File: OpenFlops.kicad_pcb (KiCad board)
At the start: 2 copper layers, 111.6 x 59.4 mm, 87 parts, among them J99 OSHW_LOGO, P1 FLOPPY_CONN, P2 POWER_INPUT, P3 USB_A_FEMALE, P4 PROG_PORT, P5 JUMPER_JC, P6 ENCODER_PORT, P7 DISPLAY_PORT, P8 USB_HEADER, P9 EXTERNAL_SPEAKER, Q1 BSS138, Q2 BSS138, Q3 BSS138, Q4 BSS138, Q5 BSS138, Q6 BSS138, Q7 MMBT3904, U1 74HCT04, U3 STM32F105RBT6, U4 LM1117-3.3, Y1 8 MHz

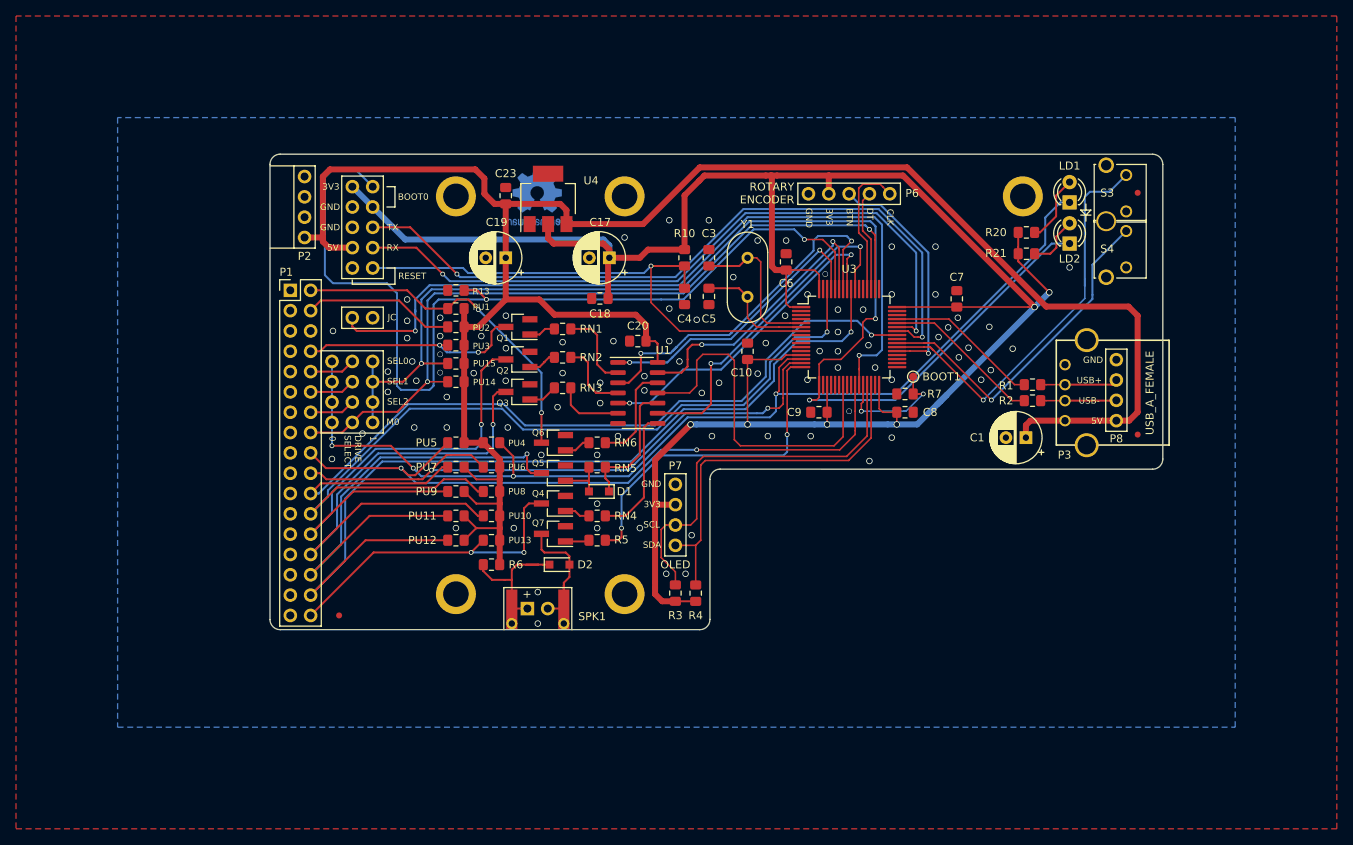
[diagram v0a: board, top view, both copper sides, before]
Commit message: Merge SD card changes from @COREi64; update to KiCad v8
This includes https://github.com/SukkoPera/OpenFlops/pull/18 from @COREi64 and updates the file formats to KiCad v8
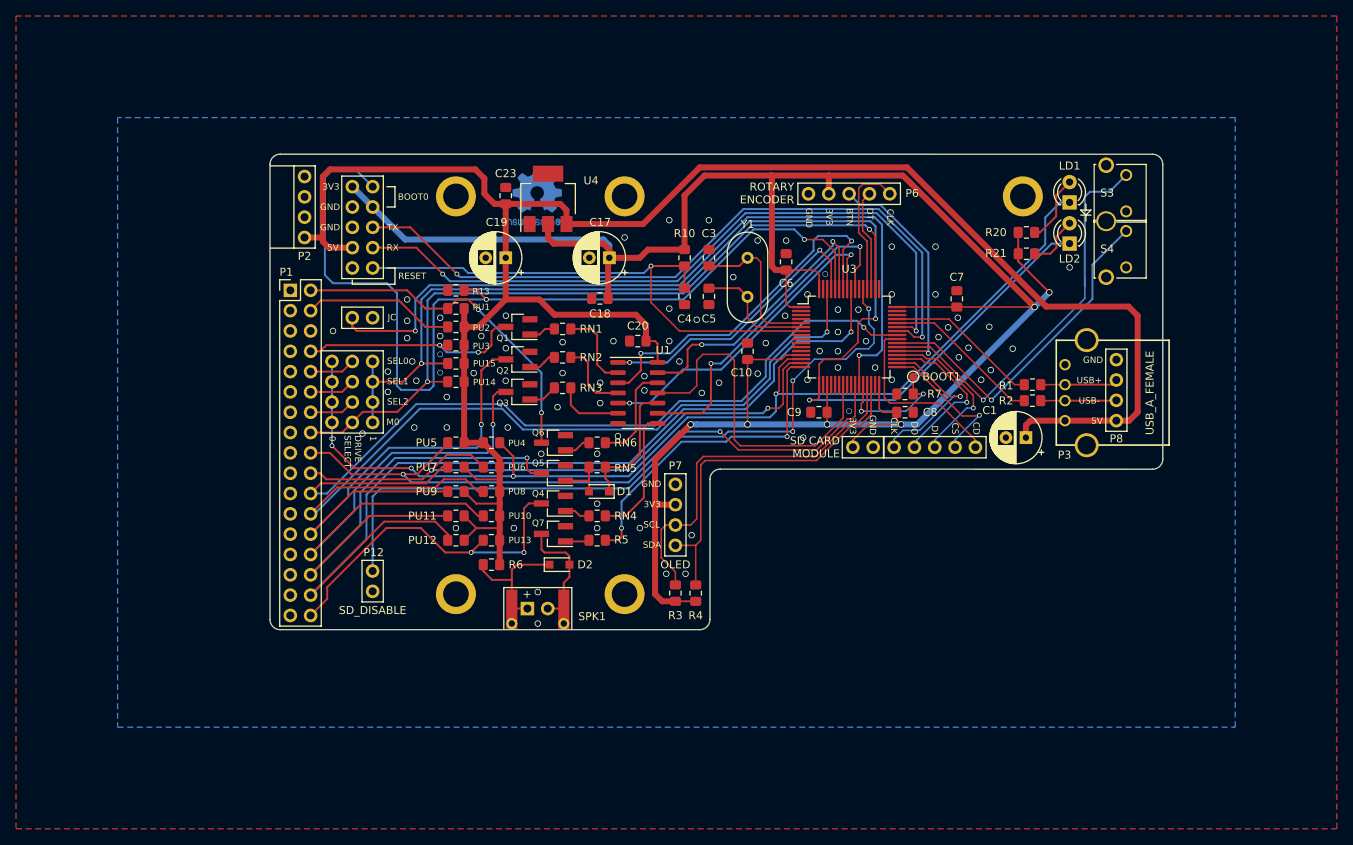
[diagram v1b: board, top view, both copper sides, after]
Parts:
- removed FID1, FID2, FID3: Fiducial, Fiducial:Fiducial_0.75mm_Mask1.5mm
- added P10: SD CARD, OpenFlops:PinHeader_1x05_P2.54mm_Vertical, F.Cu at (183.4, 92.0)
- added P11: SD PWR, OpenFlops:PinHeader_1x02_P2.54mm_Vertical, F.Cu at (170.7, 92.0)
- added P12: SD_DISABLE, OpenFlops:PinHeader_1x02_P2.54mm_Vertical, F.Cu at (108.1, 107.5)
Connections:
- net /~dskchg renamed /~{dskchg}
- net /~dskchg_3v3 renamed /~{dskchg_3v3}
- net /~index renamed /~{index}
- net /~index_3v3 renamed /~{index_3v3}
- net /~inuse renamed /~{inuse}
- net /~mtron renamed /~{mtron}
- net /~rdata renamed /~{rdata}
- net /~rdata_3v3 renamed /~{rdata_3v3}
- net /~rdy renamed /~{rdy}
- net /~rdy_3v3 renamed /~{rdy_3v3}
- net /~sel0 renamed /~{sel0}
- net /~sel1 renamed /~{sel1}
- net /~sel2 renamed /~{sel2}
- net /~selx renamed /~{selx}
- net /~sely renamed /~{sely}
- net /~side renamed /~{side}
- net /~step renamed /~{step}
- net /~trk0 renamed /~{trk0}
- net /~trk0_3v3 renamed /~{trk0_3v3}
- net /~wdata renamed /~{wdata}
- net /~wgate renamed /~{wgate}
- net /~wprot renamed /~{wprot}
- net /~wprot_3v3 renamed /~{wprot_3v3}
- P1 pad 6: (no net) -> /~{sel3}
- P2 pad 4: (no net) -> unconnected-(P2-Pad4)
- U3 pad 10: (no net) -> unconnected-(U3-Pad10)
- U3 pad 11: (no net) -> unconnected-(U3-Pad11)
- U3 pad 20: (no net) -> unconnected-(U3-Pad20)
- U3 pad 21: (no net) -> unconnected-(U3-Pad21)
- U3 pad 22: (no net) -> unconnected-(U3-Pad22)
- U3 pad 24: (no net) -> unconnected-(U3-Pad24)
- U3 pad 25: (no net) -> unconnected-(U3-Pad25)
- U3 pad 33: (no net) -> /spi_cs
- U3 pad 34: (no net) -> /spi_clk
- U3 pad 35: (no net) -> /spi_do
- U3 pad 36: (no net) -> /spi_di
- U3 pad 40: (no net) -> /spi_cd
- U3 pad 46: (no net) -> unconnected-(U3-Pad46)
- U3 pad 49: (no net) -> /swclk
- U3 pad 53: GND -> Net-(U3-Pad53)
- U3 pad 54: (no net) -> unconnected-(U3-Pad54)
- U3 pad 8: (no net) -> unconnected-(U3-Pad8)
- U3 pad 9: (no net) -> unconnected-(U3-Pad9)
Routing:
- net Net-(U3-Pad53): track 0.00 -> 91.0 mm, vias 0 -> 3
- net /spi_cd: track 0.00 -> 23.3 mm
- net /spi_clk: track 0.00 -> 21.1 mm, vias 0 -> 1
- net /spi_do: track 0.00 -> 20.8 mm, vias 0 -> 1
- net /spi_di: track 0.00 -> 20.6 mm, vias 0 -> 1
- net /spi_cs: track 0.00 -> 18.1 mm, vias 0 -> 1
- net +3V3: track 288.7 -> 296.7 mm
- net /~{rdy}: track 40.7 -> 43.4 mm
- net /~{rdata}: track 60.9 -> 59.1 mm
- net /spk+: track 18.6 -> 16.8 mm
- net /disp_dio: track 47.4 -> 45.7 mm
- net /disp_clk: track 49.0 -> 47.4 mm
- net /jb: track 42.4 -> 40.9 mm
- net /jc: track 99.9 -> 98.4 mm
- net /~{rdata_3v3}: track 44.8 -> 43.5 mm
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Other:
- net class Default removed
- net class Power removed
- net class uC removed
- board text added: "CD"
- board text added: "CS"
- board text added: "DI"
- board text added: "DO"
- board text added: "Licensed under CERN OHL v.1.3"
- board text added: "SD CARD MODULE"
- board text added: "V1.4"
- board text removed: "Licensed under CERN OHL v.1.2"
- board text removed: "V1"

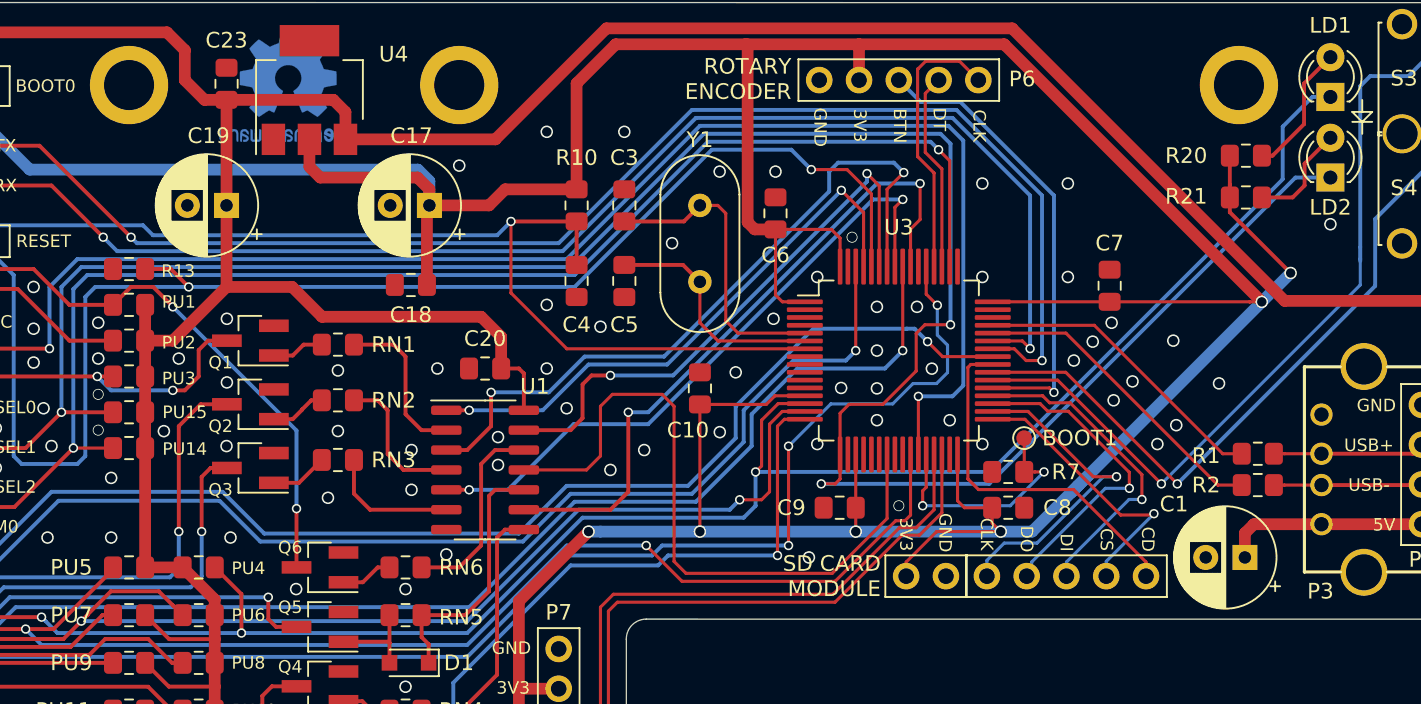
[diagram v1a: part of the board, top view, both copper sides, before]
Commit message: Change C1, C17 and C19 to SMD parts
This commit changes C1, C17 and C19 to SMD electrolytic capacitors. The Panasonic FT series (see https://industrial.panasonic.com/cdbs/www-data/pdf/RDE0000/ABA0000C1240.pdf) has both 10µF and 100µF available with 5x5.8 packages, so these are the used footprints.
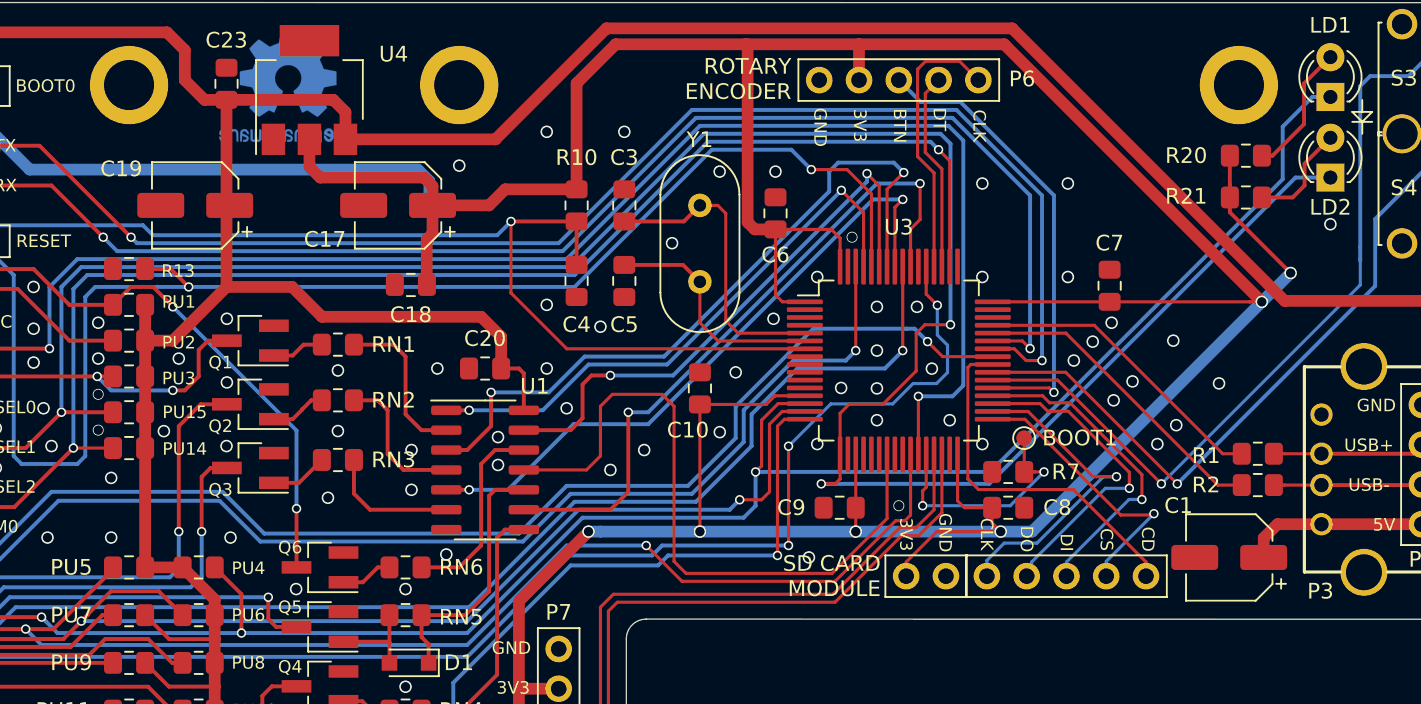
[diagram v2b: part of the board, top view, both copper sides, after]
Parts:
- C1, C17, C19: footprint Capacitor_THT:CP_Radial_D6.3mm_P2.50mm -> Capacitor_SMD:CP_Elec_5x5.8
- moved C17 2.00 mm to (135.7, 68.3)
- moved C19 2.00 mm to (122.7, 68.3)
- moved C1 1.00 mm to (188.7, 90.8)
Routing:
- net +5V: track 256.2 -> 255.0 mm

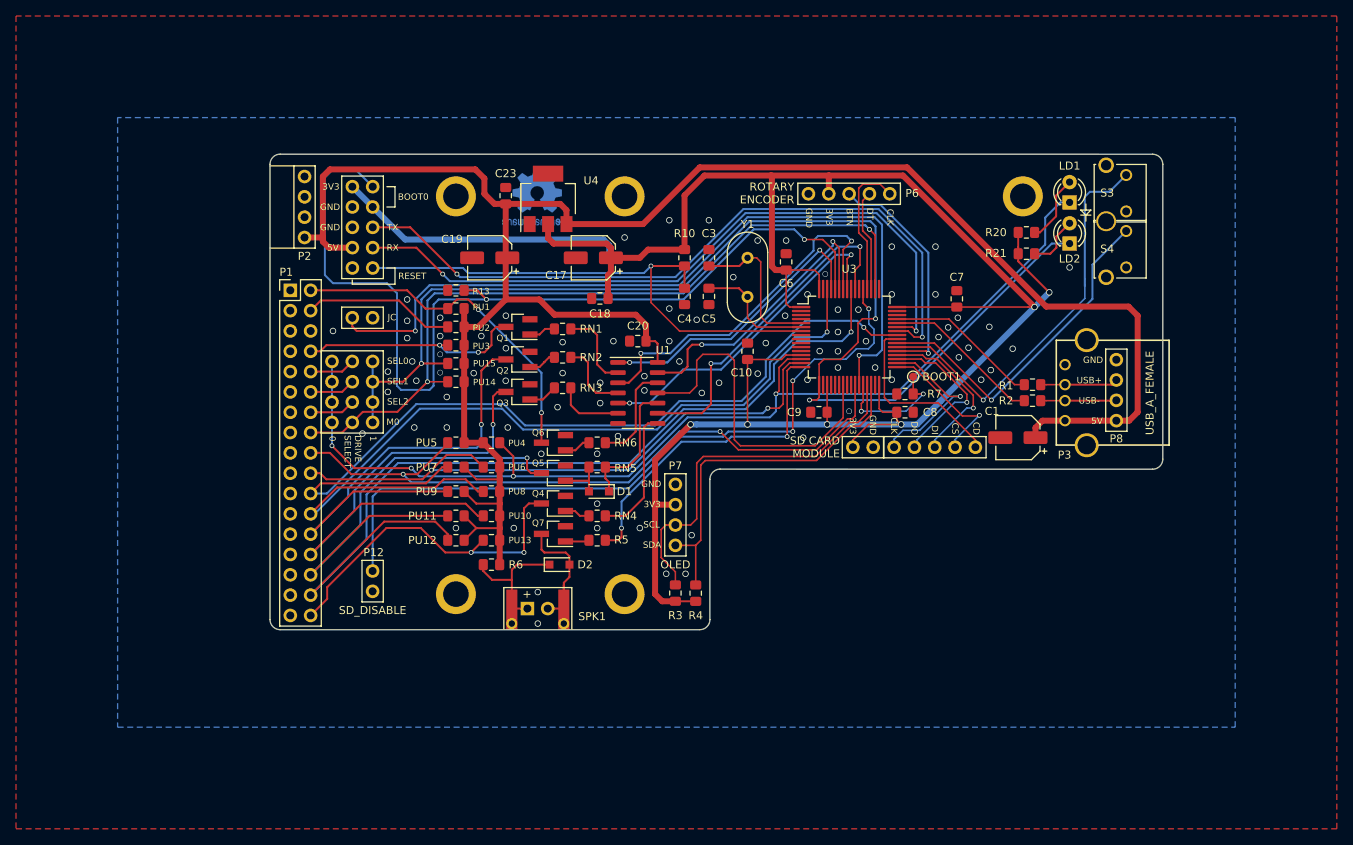
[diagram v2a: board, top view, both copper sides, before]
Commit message: Major rerouting Still not completely satisfied though
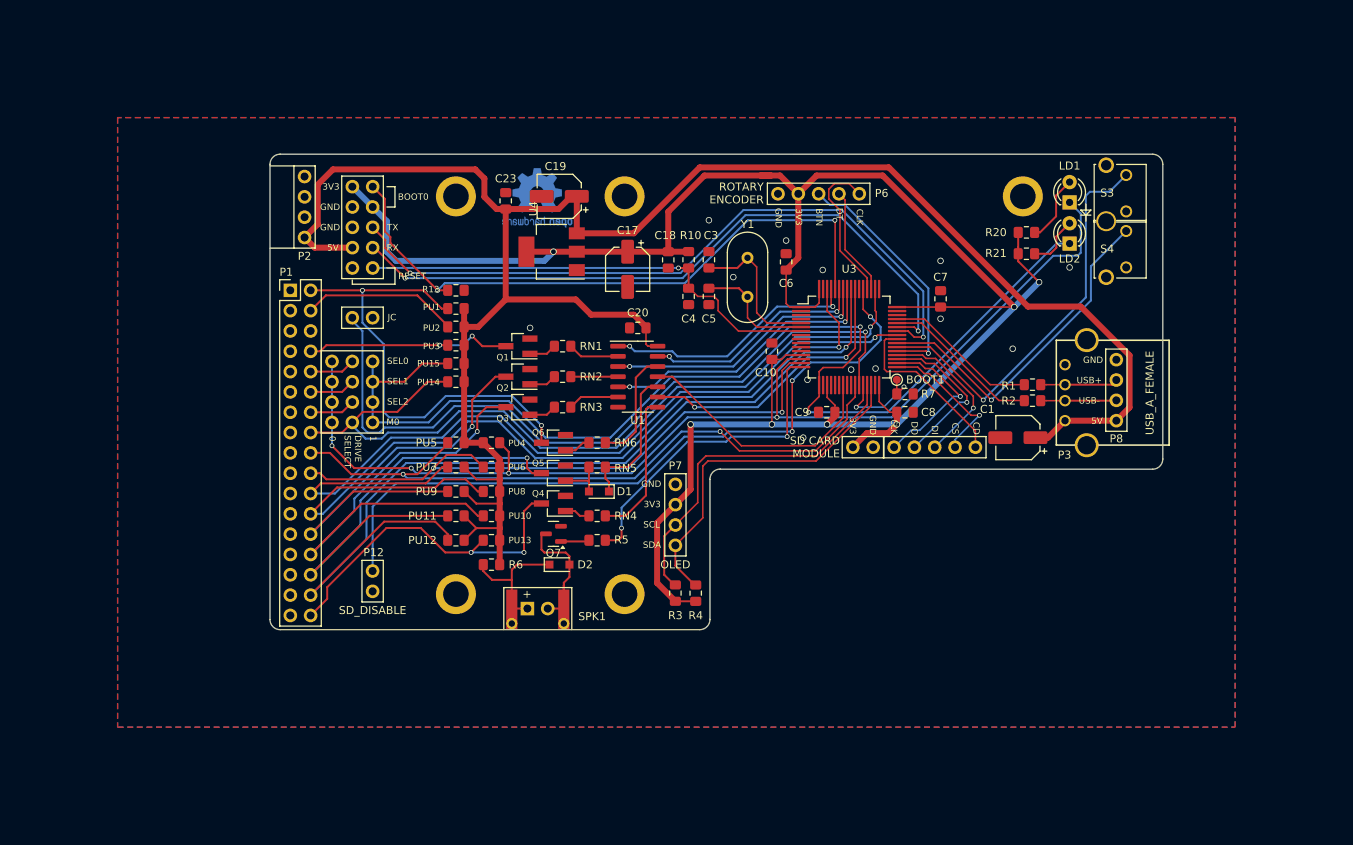
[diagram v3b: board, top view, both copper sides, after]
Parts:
- Q7: footprint Package_TO_SOT_SMD:SOT-23_Handsoldering -> Package_TO_SOT_SMD:SOT-23
- moved C19 11.6 mm to (131.4, 60.6)
- moved C18 9.81 mm to (145.0, 68.6), turned to -90 degrees
- moved U4 6.62 mm to (130.5, 67.6), turned to 180 degrees
- moved C17 4.52 mm to (140.0, 69.8), turned to -90 degrees
- moved P6 3.81 mm to (158.8, 60.3)
- moved C10 3.05 mm to (158.0, 80.0)
- moved RN3 2.41 mm to (131.8, 87.0)
- moved Q1 2.41 mm to (126.2, 79.4)
- moved RN2 2.41 mm to (131.8, 83.2)
- moved Q2 2.16 mm to (126.2, 83.2)
- moved RN1 2.16 mm to (131.8, 79.4)
- moved TP1 2.08 mm to (173.6, 83.6)
- moved C7 2.03 mm to (179.1, 73.5)
- moved U1 2.03 mm to (141.2, 83.2)
- moved Q3 1.91 mm to (126.2, 87.0)
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- renumbered J99 to V0
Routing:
- net /boot0: track 119.5 -> 81.6 mm
- net +3V3: track 297.1 -> 264.1 mm, vias 6 -> 7
- net /~{dskchg}: track 42.8 -> 59.2 mm
- net /~{trk0_3v3}: track 45.8 -> 34.1 mm
- net /~{sely}: track 155.2 -> 143.5 mm, vias 3 -> 2
- net /~{rdata_3v3}: track 43.5 -> 32.6 mm
- net /~{dskchg_3v3}: track 36.9 -> 28.1 mm
- net /nrst: track 67.5 -> 59.0 mm
- net /~{rdy_3v3}: track 42.8 -> 35.5 mm
- net /~{wprot_3v3}: track 41.6 -> 35.8 mm
- net /jc: track 98.4 -> 92.9 mm, vias 2 -> 1
- net +5V: track 255.0 -> 249.8 mm
- net /~{index_3v3}: track 36.8 -> 32.2 mm
- net /~{trk0}: track 58.4 -> 53.8 mm
- net /~{selx}: track 133.6 -> 138.0 mm
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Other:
- board text added: "V2"
- board text removed: "V1.4"
